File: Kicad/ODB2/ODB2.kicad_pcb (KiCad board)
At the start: 4 copper layers, 83.9 x 76.5 mm, 184 parts, among them J4 RF2-04A-T-00-50-G, J5 RFM_Conn_Coaxial, U1 STM32F412ZGTx, U10 W25Q512JVEIQ, U2 TLV2371DBV, U3 74LV1T87GVH, U5 L76L-M33, U6 ICM-20948, U7 MS580301BA01-00

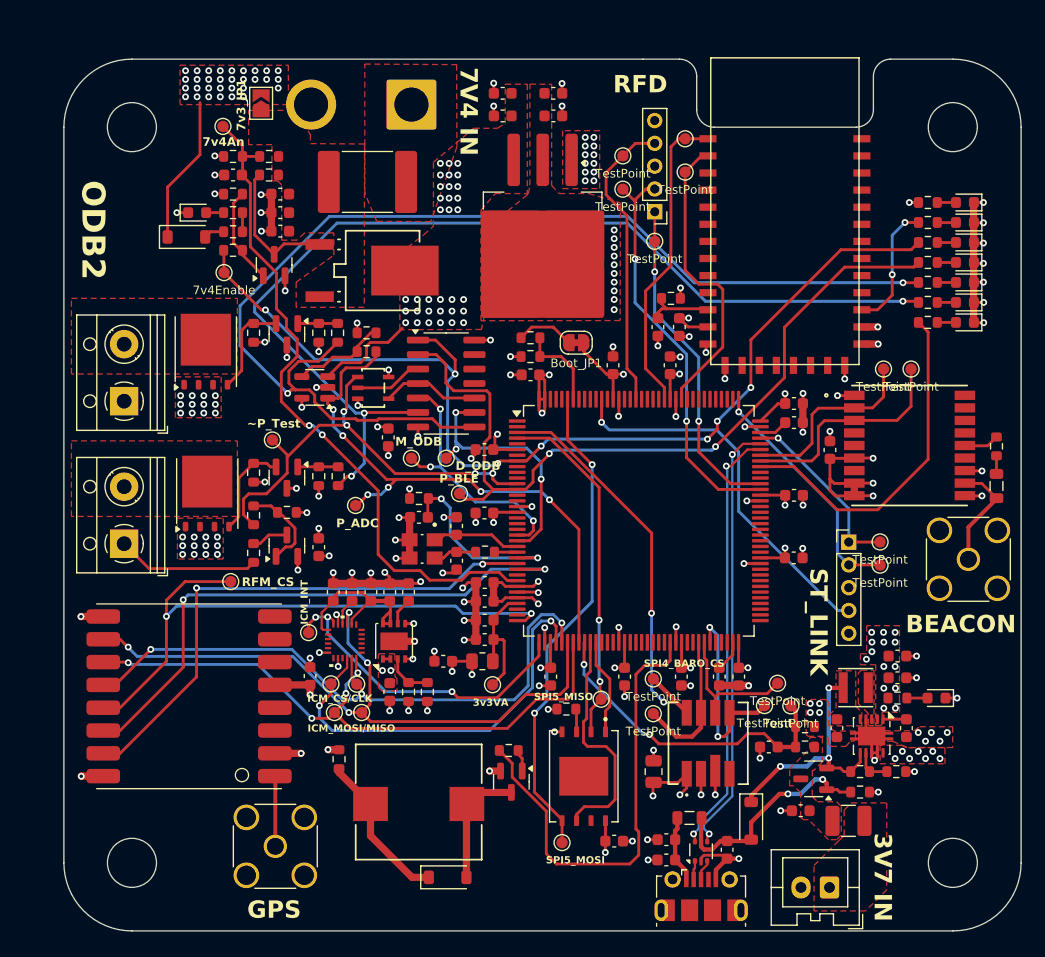
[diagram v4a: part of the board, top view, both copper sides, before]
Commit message: déplacement led ble connection + fixes DRC usb
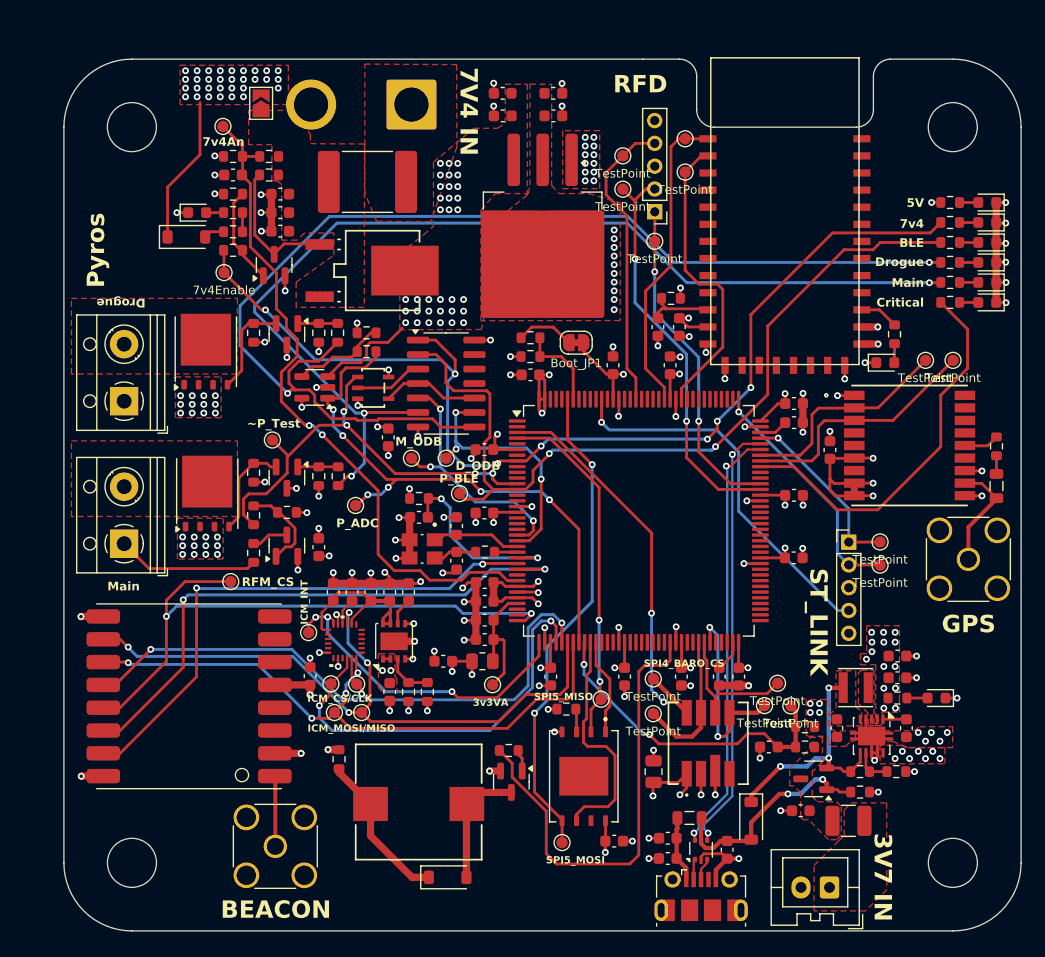
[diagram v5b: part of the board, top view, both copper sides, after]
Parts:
- moved BT_LED1 14.1 mm to (72.0, 26.6), turned to 0 degrees
- moved BT_R2 10.2 mm to (72.8, 24.1), turned to -90 degrees
- moved TP7 3.76 mm to (78.0, 26.4)
- moved TP8 3.76 mm to (75.6, 26.4)
- moved CLED_R1 2.63 mm to (77.7, 21.3)
- moved Pyros_R18 2.63 mm to (77.7, 17.8)
- moved Pyros_R19 2.63 mm to (77.7, 16.1)
- moved 7v4_R8 2.63 mm to (77.7, 14.3)
- moved Pyros_R17 2.63 mm to (77.7, 19.6)
- moved CLED_LED1 2.63 mm to (81.0, 21.3)
- moved Pyros_LED2 2.63 mm to (81.0, 17.8)
- moved Pyros_LED4 2.63 mm to (81.0, 16.1)
- moved LED_7v4Enable1 2.63 mm to (81.0, 14.3)
- moved Pyros_LED1 2.63 mm to (81.0, 19.6)
- moved 5v_R1 1.96 mm to (77.7, 12.6)
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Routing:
- net Net-(E1-LED): track 11.2 -> 3.41 mm, vias 2 -> 0
- net 7v4Enable: track 90.9 -> 94.9 mm
- net CriticalLEDEnable: track 30.5 -> 34.3 mm
- net Pyros_Bluetooth: track 69.9 -> 73.5 mm
- net UART1_GPS_RX: track 16.8 -> 19.4 mm
- net UART1_GPS_TX: track 19.9 -> 22.0 mm
- net +5V: track 17.8 -> 19.7 mm
- net GND: track 156.4 -> 154.9 mm
- net Pyros_DrogueOn: track 100.0 -> 101.3 mm
- net Pyros_MainOn: track 90.2 -> 91.4 mm
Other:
- board text added: "5V"
- board text added: "7v4"
- board text added: "BLE"
- board text added: "Critical"
- board text added: "Drogue"
- board text added: "Main"
- board text added: "Pyros"
- board text removed: "7v3_JP1"
- board text removed: "ODB2"

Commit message: silkscreens
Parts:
- moved TP30 1.85 mm to (62.3, 58.3)
- moved TP27 1.71 mm to (61.3, 55.8)
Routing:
- net SPI4_Baro_MISO: track 12.5 -> 10.8 mm
- net SPI4_Baro_MOSI: track 17.4 -> 18.4 mm
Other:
- board text added: "10"
- board text added: "11"
- board text added: "12"
- board text added: "13"
- board text added: "14"
- board text added: "15"
- board text added: "17"
- board text added: "18"
- board text added: "19"
- board text added: "2"
- board text added: "20"
- board text added: "21"
- board text added: "3"
- board text added: "3v7_An"
- board text added: "4"
- board text added: "5"
- board text added: "6"
- board text added: "7"
- board text added: "8"
- board text added: "9"
- board text removed: "D_ODB"
- board text removed: "ICM_CS/CLK"
- board text removed: "ICM_INT"
- board text removed: "ICM_MOSI/MISO"
- board text removed: "M_ODB"
- board text removed: "P_ADC"
- board text removed: "P_BLE"
- board text removed: "RFM_CS"
- board text removed: "SPI4_BARO_CS"
- board text removed: "SPI5_MISO"
- board text removed: "SPI5_MOSI"
- board text removed: "~P_Test"

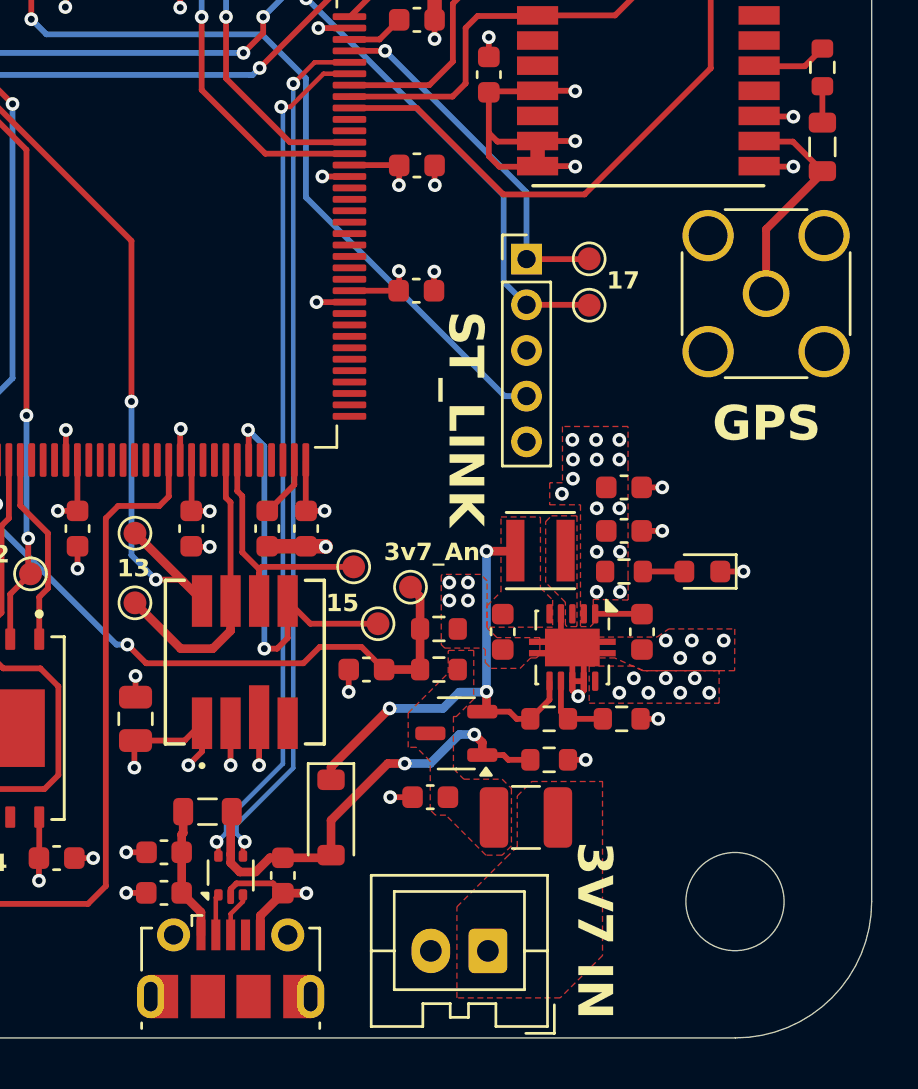
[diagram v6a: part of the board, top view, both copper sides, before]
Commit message: déplacement usb (pcb edge) + changement 3v7 connector
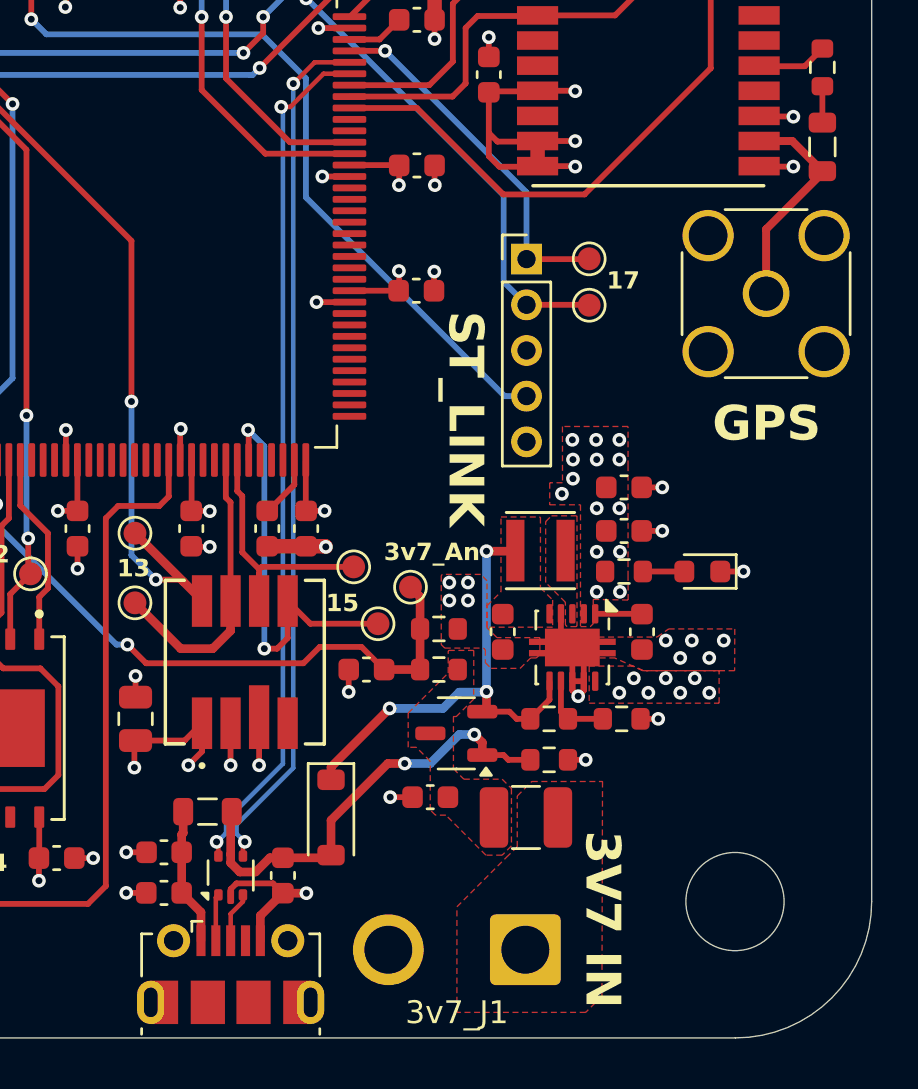
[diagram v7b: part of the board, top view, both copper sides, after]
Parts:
- 3v7_J1: footprint Connector_JST:JST_XA_B02B-XASK-1_1x02_P2.50mm_Vertical -> Connector_Wire:SolderWire-1.5sqmm_1x02_P6mm_D1.7mm_OD3mm
- TP2: value INT -> TestPoint
- TP21: value 7v4Enable -> TestPoint
- TP3: value CS -> TestPoint
- moved 3v7_J1 1.64 mm to (68.8, 72.6)
- moved USB_Bus1 0.25 mm to (55.9, 73.7)

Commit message: ajout M. Nathan silkscreen
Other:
- board text added: "Luka Dupuis Samuel Gagnon Mathis Tremblay Victor Deschênes Brieuc Soriano-Lohéac Nathan Armishaw 02-2025 V1"
- board text removed: "Luka Dupuis Samuel Gagnon Mathis Tremblay Victor Deschênes Brieuc Soriano-Lohéac 02-2025 V1"
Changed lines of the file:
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@@
 		(layer "Edge.Cuts")
 	)
-	(gr_text "Luka Dupuis\nSamuel Gagnon\nMathis Tremblay\nVictor Deschênes\nBrieuc Soriano-Lohéac\n\n02-2025 V1"
+	(gr_text "Luka Dupuis\nSamuel Gagnon\nMathis Tremblay\nVictor Deschênes\nBrieuc Soriano-Lohéac\nNathan Armishaw\n\n02-2025 V1"
 		(at 72.39 9.398 90)
 		(layer "B.SilkS")
